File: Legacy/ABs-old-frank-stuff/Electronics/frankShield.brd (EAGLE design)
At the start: 31.1 x 16.5 mm, 9 parts

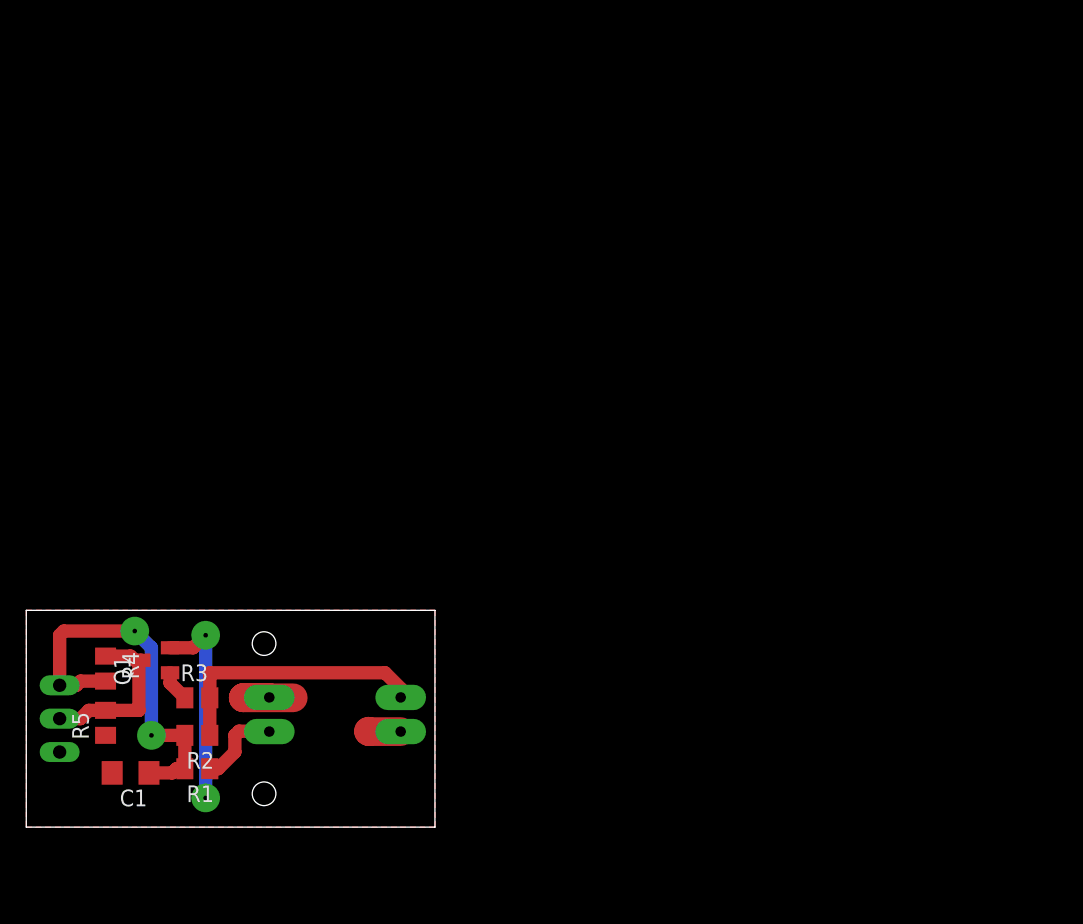
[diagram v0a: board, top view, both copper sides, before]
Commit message: PCBs corrected (D9 now LED) and improved (wheel sensor has 4 mounting holes); software updated to match.
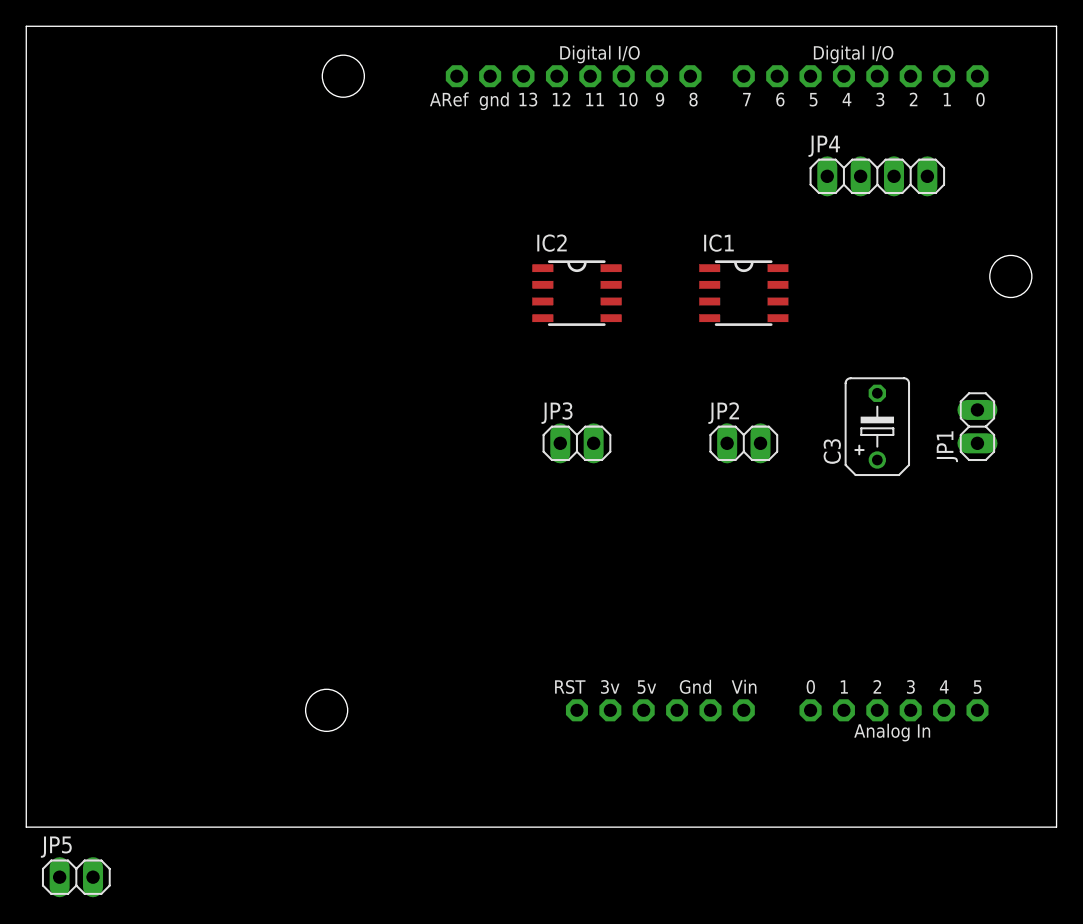
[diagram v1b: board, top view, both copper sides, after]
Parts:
- removed C1: 10uF, rcl:C1206
- removed Q1: (no value), adafruit:SOT23
- removed R1: 120R, rcl:M0805
- removed R2: 1K8, rcl:M0805
- removed R3: 10K, rcl:M0805
- removed R4: 1K2, rcl:M0805
- removed R5: 1K, rcl:M0805
- added C3: 1000uF, rcl:B45181B
- added IC1, IC2: BD6230F, rohm:SOP8
- added JP2, JP3, JP5: (no value), pinhead:1X02
- added JP4: (no value), pinhead:1X04
- JP1: device pinhead:1X03 -> pinhead:1X02
- U$1: value RPI-579N1 -> ARDUINO-BPLACE; device reprapltd:RPI-579N1 -> adafruit:ARDUINO-BPLACE
- moved JP1 73.3 mm to (72.4, 30.5), flipped to the top, turned to 90 degrees
- moved U$1 14.8 mm to (8.89, 6.35), flipped to the top, turned to 0 degrees
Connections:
- new net 5V: U$1.5V
- new net GND2: U$1.GND2
- new net N$10: IC2.5, U$1.D8
- new net N$4: IC1.7, JP2.2
- new net N$6: IC2.7, JP3.2
- new net N$7: IC1.5, U$1.D5
- new net N$8: IC1.4, U$1.D6
- new net N$9: IC2.4, U$1.D7
- new net V+: C3.+, IC1.2, IC1.3, IC1.6, IC2.2, IC2.3, IC2.6, JP1.2, JP5.1
- new net VIN: U$1.VIN
- net +3V3: now also JP4.2, U$1.3V; no longer C1.1, JP1.1, R1.2, R2.2, R4.2
- net GND: now also C3.-, IC1.8, IC2.8, JP1.1, JP4.1, JP5.2, U$1.GND, U$1.GND1; no longer C1.2, JP1.3, Q1.2, R5.1, U$1.P$2, U$1.P$4
- net N$1: now also JP4.4, U$1.D3; no longer JP1.2, Q1.3, R4.1, R5.2
- net N$2: now also JP4.3, U$1.D4; no longer R1.1, U$1.P$1
- net N$3: now also IC1.1, JP2.1; no longer Q1.1, R3.1
- net N$5: now also IC2.1, JP3.1; no longer R2.1, R3.2, U$1.P$3
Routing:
- net +3V3: track 29.7 -> 0.00 mm, vias 2 -> 0
- net GND: track 23.8 -> 0.00 mm, vias 2 -> 0
- net N$5: track 20.5 -> 0.00 mm
- net N$1: track 13.0 -> 0.00 mm
- net N$2: track 6.47 -> 0.00 mm
- net N$3: track 2.37 -> 0.00 mm
- removed copper zone on layer 1, net GND
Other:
- board size 31.1 x 16.5 mm -> 78.4 x 61 mm
